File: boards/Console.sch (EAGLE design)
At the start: 27 parts, among them IC1 PIC18F4550_40, X3 PN61729-S

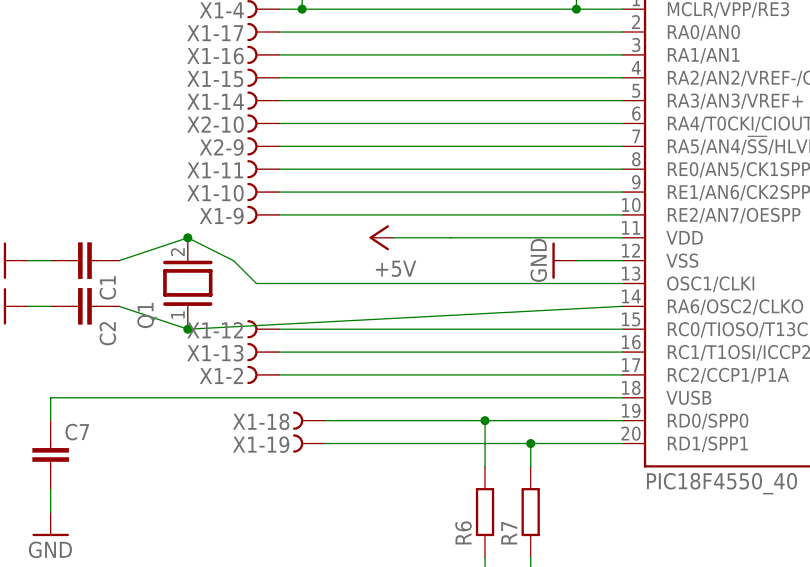
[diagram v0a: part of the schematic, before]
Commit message: Reader: Added new service
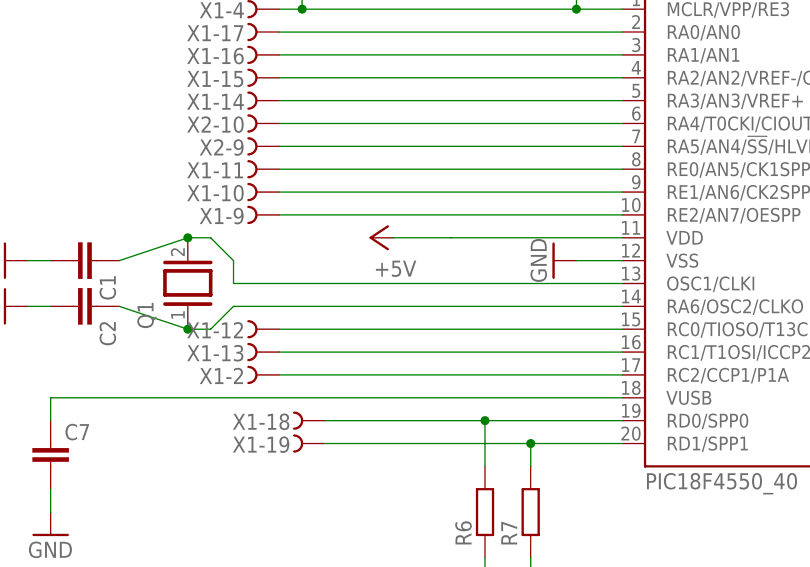
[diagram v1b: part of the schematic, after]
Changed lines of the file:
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@@
 <setting verticaltext="up"/>
 </settings>
-<grid distance="0.05" unitdist="inch" unit="inch" style="lines" multiple="1" display="no" altdistance="0.01" altunitdist="inch" altunit="inch"/>
+<grid distance="0.1" unitdist="inch" unit="inch" style="lines" multiple="1" display="no" altdistance="0.01" altunitdist="inch" altunit="inch"/>
 <layers>
 <layer number="1" name="Top" color="4" fill="1" visible="no" active="no"/>
@@
 <wire x1="-81.28" y1="15.24" x2="-73.66" y2="12.7" width="0.1524" layer="91"/>
 <pinref part="IC1" gate="G$1" pin="RA6/OSC2/CLKO"/>
-<wire x1="-25.4" y1="15.24" x2="-73.66" y2="12.7" width="0.1524" layer="91"/>
+<wire x1="-25.4" y1="15.24" x2="-68.58" y2="15.24" width="0.1524" layer="91"/>
+<wire x1="-68.58" y1="15.24" x2="-71.12" y2="12.7" width="0.1524" layer="91"/>
+<wire x1="-71.12" y1="12.7" x2="-73.66" y2="12.7" width="0.1524" layer="91"/>
 <pinref part="C2" gate="G$1" pin="1"/>
 <junction x="-73.66" y="12.7"/>
@@
 <pinref part="C1" gate="G$1" pin="1"/>
 <pinref part="IC1" gate="G$1" pin="OSC1/CLKI"/>
-<wire x1="-25.4" y1="17.78" x2="-66.04" y2="17.78" width="0.1524" layer="91"/>
-<wire x1="-66.04" y1="17.78" x2="-68.58" y2="20.32" width="0.1524" layer="91"/>
-<wire x1="-68.58" y1="20.32" x2="-73.66" y2="22.86" width="0.1524" layer="91"/>
+<wire x1="-25.4" y1="17.78" x2="-68.58" y2="17.78" width="0.1524" layer="91"/>
+<wire x1="-68.58" y1="17.78" x2="-68.58" y2="20.32" width="0.1524" layer="91"/>
+<wire x1="-68.58" y1="20.32" x2="-71.12" y2="22.86" width="0.1524" layer="91"/>
+<wire x1="-71.12" y1="22.86" x2="-73.66" y2="22.86" width="0.1524" layer="91"/>
 <junction x="-73.66" y="22.86"/>
 </segment>
